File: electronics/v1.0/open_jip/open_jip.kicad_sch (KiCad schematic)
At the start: 28 parts, among them Q1 BSS214NW, U1 OPA355NA, U2 OPA355NA, U3 DAC5571IDBVR, U4 OPA355NA, U5 SeeeduinoXIAO

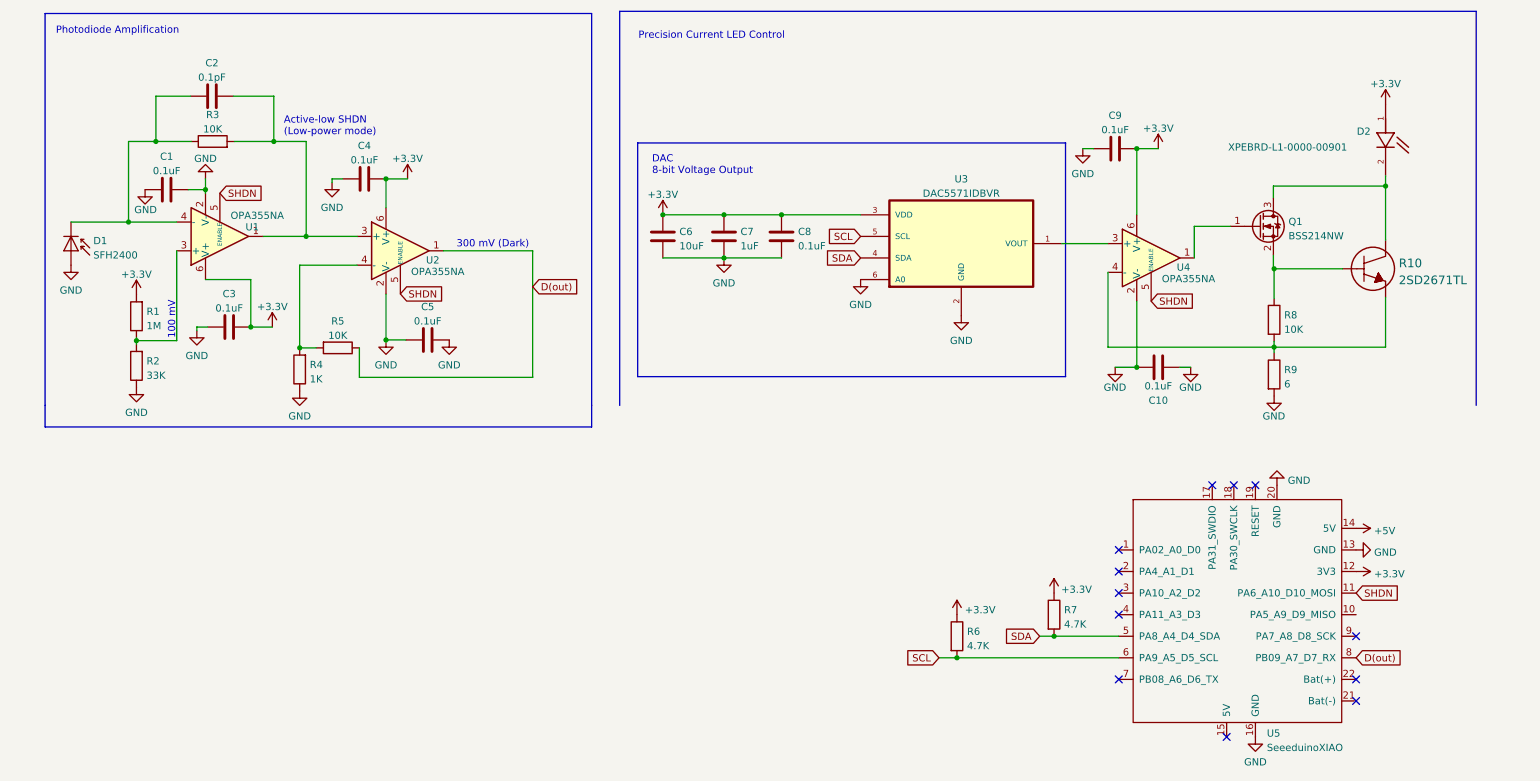
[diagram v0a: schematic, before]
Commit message: added some prelim firmware for v1.0, updated schematic and pcb to remove the second stage trans impedance amplifier on both detection excitation
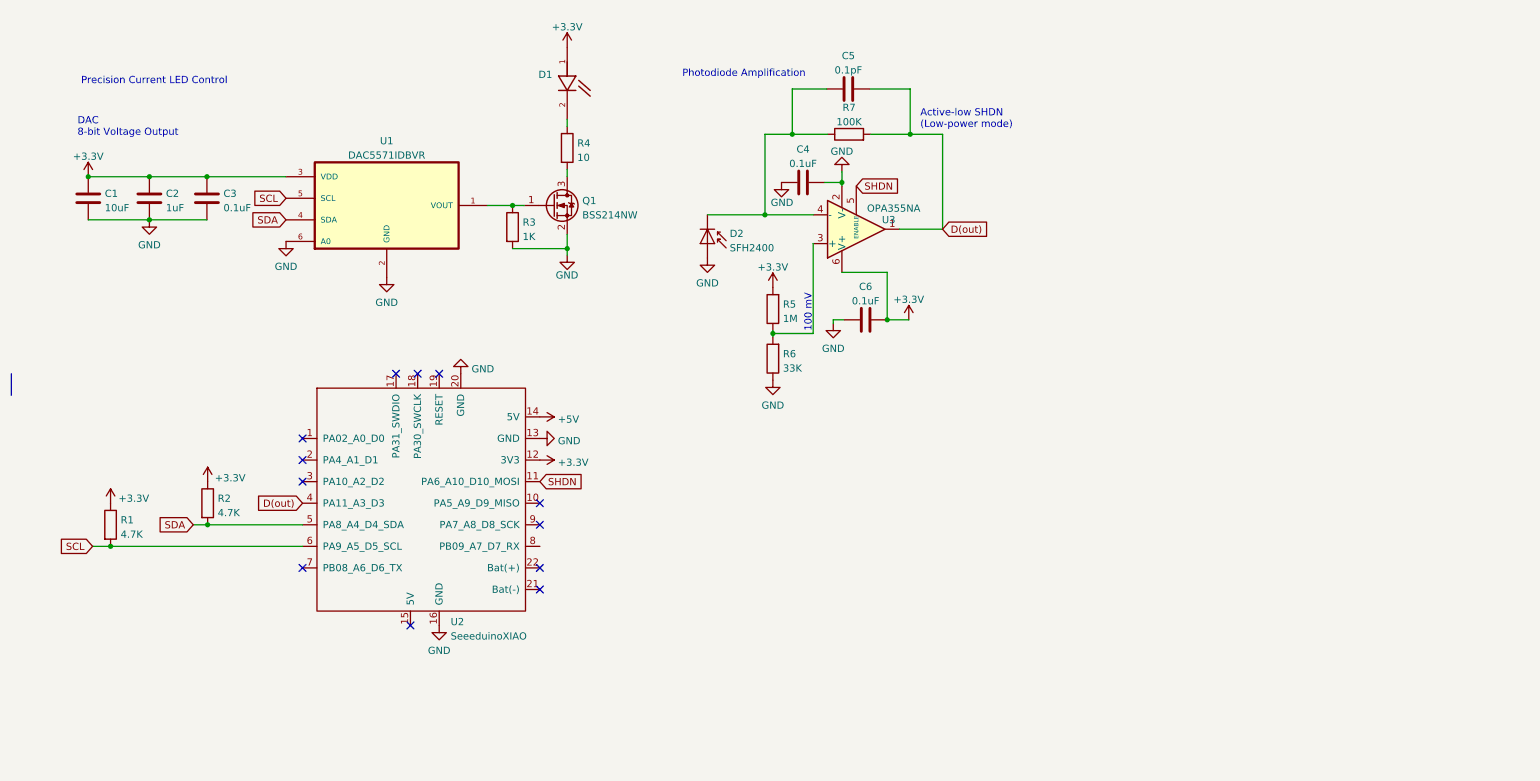
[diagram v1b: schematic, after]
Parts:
- removed C10, C4, C5, C9: 0.1uF, Capacitor_SMD:C_0805_2012Metric, symbol Device:C
- removed R10: 2SD2671TL, 2SD2671TL:2SD2671TL, symbol 2SD2671TL:2SD2671TL
- removed R4: 1K, Resistor_SMD:R_0805_2012Metric, symbol Device:R
- removed R5, R8: 10K, Resistor_SMD:R_0805_2012Metric, symbol Device:R
- removed U2, U4: OPA355NA, Package_TO_SOT_SMD:SOT-23-6, symbol Amplifier_Operational:OPA355NA
- added R3: 1K, Resistor_SMD:R_0805_2012Metric, symbol Device:R
- R4: renamed from R9; value 6 -> 10
- R7: renamed from R3; value 10K -> 100K
- renumbered C6 to C1, C7 to C2, C8 to C3, C1 to C4, C2 to C5, C3 to C6, D2 to D1, D1 to D2, R6 to R1, R7 to R2, R1 to R5, R2 to R6, U3 to U1, U5 to U2, U1 to U3
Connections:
- net D(out): now also C5.2, R7.2, U2.4 (PA11_A3_D3), U3.1; no longer U2.8 (PB09_A7_D7_RX)
- net GND: now also Q1.2 (S), R3.2; no longer R4.2
- net at U1.1 (VOUT): now also Q1.1 (G), R3.1
- net at Q1.3 (D): now also R4.2; no longer D1.2
- net at R4.1: now also D1.2
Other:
- note removed: "300 mV (Dark)"
- moved on the sheet: C1, C2, C3, C4, C5, C6, D1, D2, Q1, R1, R2, R4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

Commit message: sent of two versions to be manufactured, one smd photodiode other with tht
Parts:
- removed C4: 0.1uF, Capacitor_SMD:C_0805_2012Metric, symbol Device:C
- removed D2: SFH2400, OptoDevice:Osram_SMD-SmartDIL, symbol Sensor_Optical:SFH2400
- added D2: SFH_213_FA, SFH_213_FA:XDCR_SFH_213_FA, symbol SFH_213_FA:SFH_213_FA
- R4: value 10 -> 2
- renumbered C5 to C4, C6 to C5
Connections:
- net GND: now also D2.1
- net at C4.1, R7.1, U3.4 (-): now also D2.2
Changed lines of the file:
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@@
   (junction (at 52.197 109.347) (diameter 0) (color 0 0 0 0)
-  )
-  (junction (at 164.211 48.895) (diameter 0) (color 0 0 0 0)
   )
   (junction (at 35.052 113.157) (diameter 0) (color 0 0 0 0)
@@
     (stroke (width 0) (type default) (color 0 0 0 0))
   )
-  (wire (pts (xy 161.163 48.895) (xy 164.211 48.895))
-    (stroke (width 0) (type default) (color 0 0 0 0))
-  )
   (wire (pts (xy 159.131 75.565) (xy 159.131 59.69))
     (stroke (width 0) (type default) (color 0 0 0 0))
@@
     (stroke (width 0) (type default) (color 0 0 0 0))
   )
-  (wire (pts (xy 164.211 48.895) (xy 164.211 49.53))
+  (wire (pts (xy 164.211 46.99) (xy 164.211 49.53))
     (stroke (width 0) (type default) (color 0 0 0 0))
   )
@@
   )
   (wire (pts (xy 176.276 40.386) (xy 181.991 40.386))
-    (stroke (width 0) (type default) (color 0 0 0 0))
-  )
-  (wire (pts (xy 164.211 46.99) (xy 164.211 48.895))
     (stroke (width 0) (type default) (color 0 0 0 0))
   )
@@
   (symbol (lib_id "power:+3.3V") (at 176.022 73.152 0) (unit 1)
     (in_bom yes) (on_board yes) (fields_autoplaced)
-    (property "Reference" "#PWR020" (id 0) (at 176.022 76.962 0)
+    (property "Reference" "#PWR019" (id 0) (at 176.022 76.962 0)
       (effects (font (size 1.27 1.27)) hide)
     )
@@
     (pin "1")
   )
-  (symbol (lib_id "power:GND") (at 140.462 62.23 0) (unit 1)
-    (in_bom yes) (on_board yes) (fields_autoplaced)
-    (property "Reference" "#PWR014" (id 0) (at 140.462 68.58 0)
-      (effects (font (size 1.27 1.27)) hide)
-    )
-    (property "Value" "GND" (id 1) (at 140.462 66.6734 0))
-    (property "Footprint" "" (id 2) (at 140.462 62.23 0)
-      (effects (font (size 1.27 1.27)) hide)
-    )
-    (property "Datasheet" "" (id 3) (at 140.462 62.23 0)
+  (symbol (lib_id "SFH_213_FA:SFH_213_FA") (at 140.462 59.69 90) (unit 1)
+    (in_bom yes) (on_board yes)
+    (property "Reference" "D2" (id 0) (at 142.748 60.7476 90)
+      (effects (font (size 1.27 1.27)) (justify right))
+    )
+    (property "Value" "SFH_213_FA" (id 1) (at 128.397 63.627 90)
+      (effects (font (size 1.27 1.27)) (justify right))
+    )
+    (property "Footprint" "SFH_213_FA:XDCR_SFH_213_FA" (id 2) (at 140.462 59.69 0)
+      (effects (font (size 1.27 1.27)) (justify left bottom) hide)
+    )
+    (property "Datasheet" "" (id 3) (at 140.462 59.69 0)
+      (effects (font (size 1.27 1.27)) (justify left bottom) hide)
+    )
+    (property "PARTREV" "1.3" (id 4) (at 140.462 59.69 0)
+      (effects (font (size 1.27 1.27)) (justify left bottom) hide)
+    )
+    (property "STANDARD" "Manufacturer Recommendations" (id 5) (at 140.462 59.69 0)
+      (effects (font (size 1.27 1.27)) (justify left bottom) hide)
+    )
+    (property "MANUFACTURER" "OSRAM" (id 6) (at 140.462 59.69 0)
+      (effects (font (size 1.27 1.27)) (justify left bottom) hide)
+    )
+    (pin "1")
+    (pin "2")
+  )
+  (symbol (lib_id "power:GND") (at 140.462 67.31 0) (unit 1)
+    (in_bom yes) (on_board yes) (fields_autoplaced)
+    (property "Reference" "#PWR014" (id 0) (at 140.462 73.66 0)
+      (effects (font (size 1.27 1.27)) hide)
+    )
+    (property "Value" "GND" (id 1) (at 140.462 71.7534 0))
+    (property "Footprint" "" (id 2) (at 140.462 67.31 0)
+      (effects (font (size 1.27 1.27)) hide)
+    )
+    (property "Datasheet" "" (id 3) (at 140.462 67.31 0)
       (effects (font (size 1.27 1.27)) hide)
     )
@@
   (symbol (lib_id "Device:C") (at 168.402 73.152 90) (unit 1)
     (in_bom yes) (on_board yes) (fields_autoplaced)
-    (property "Reference" "C6" (id 0) (at 168.402 67.2932 90))
+    (property "Reference" "C5" (id 0) (at 168.402 67.2932 90))
     (property "Value" "0.1uF" (id 1) (at 168.402 69.8301 90))
     (property "Footprint" "Capacitor_SMD:C_0805_2012Metric" (id 2) (at 172.212 72.1868 0)
@@
     (pin "2")
   )
-  (symbol (lib_id "Device:C") (at 157.353 48.895 90) (unit 1)
-    (in_bom yes) (on_board yes) (fields_autoplaced)
-    (property "Reference" "C4" (id 0) (at 157.353 43.0362 90))
-    (property "Value" "0.1uF" (id 1) (at 157.353 45.5731 90))
-    (property "Footprint" "Capacitor_SMD:C_0805_2012Metric" (id 2) (at 161.163 47.9298 0)
-      (effects (font (size 1.27 1.27)) hide)
-    )
-    (property "Datasheet" "~" (id 3) (at 157.353 48.895 0)
-      (effects (font (size 1.27 1.27)) hide)
-    )
-    (pin "1")
-    (pin "2")
-  )
   (symbol (lib_id "power:GND") (at 41.91 55.499 0) (unit 1)
     (in_bom yes) (on_board yes) (fields_autoplaced)
@@
   (symbol (lib_id "power:GND") (at 162.687 73.787 0) (unit 1)
     (in_bom yes) (on_board yes) (fields_autoplaced)
-    (property "Reference" "#PWR018" (id 0) (at 162.687 80.137 0)
+    (property "Reference" "#PWR017" (id 0) (at 162.687 80.137 0)
       (effects (font (size 1.27 1.27)) hide)
     )
@@
       (effects (font (size 1.27 1.27)) (justify left))
     )
-    (property "Value" "10" (id 1) (at 117.475 44.5012 0)
+    (property "Value" "2" (id 1) (at 117.475 44.5012 0)
       (effects (font (size 1.27 1.27)) (justify left))
     )
@@
   (symbol (lib_id "power:GND") (at 164.211 46.99 180) (unit 1)
     (in_bom yes) (on_board yes) (fields_autoplaced)
-    (property "Reference" "#PWR019" (id 0) (at 164.211 40.64 0)
+    (property "Reference" "#PWR018" (id 0) (at 164.211 40.64 0)
       (effects (font (size 1.27 1.27)) hide)
     )
@@
     (pin "1")
   )
-  (symbol (lib_id "power:GND") (at 153.543 48.895 0) (unit 1)
-    (in_bom yes) (on_board yes)
-    (property "Reference" "#PWR017" (id 0) (at 153.543 55.245 0)
-      (effects (font (size 1.27 1.27)) hide)
-    )
-    (property "Value" "GND" (id 1) (at 151.638 52.451 0)
-      (effects (font (size 1.27 1.27)) (justify left))
-    )
-    (property "Footprint" "" (id 2) (at 153.543 48.895 0)
-      (effects (font (size 1.27 1.27)) hide)
-    )
-    (property "Datasheet" "" (id 3) (at 153.543 48.895 0)
-      (effects (font (size 1.27 1.27)) hide)
-    )
-    (pin "1")
-  )
   (symbol (lib_id "Device:R") (at 152.019 71.247 180) (unit 1)
     (in_bom yes) (on_board yes) (fields_autoplaced)
@@
   (symbol (lib_id "Device:C") (at 165.354 32.385 90) (unit 1)
     (in_bom yes) (on_board yes) (fields_autoplaced)
-    (property "Reference" "C5" (id 0) (at 165.354 26.5262 90))
+    (property "Reference" "C4" (id 0) (at 165.354 26.5262 90))
     (property "Value" "0.1pF" (id 1) (at 165.354 29.0631 90))
     (property "Footprint" "Capacitor_SMD:C_0805_2012Metric" (id 2) (at 169.164 31.4198 0)
@@
     (pin "2")
   )
-  (symbol (lib_id "Sensor_Optical:SFH2400") (at 140.462 59.69 270) (unit 1)
-    (in_bom yes) (on_board yes) (fields_autoplaced)
-    (property "Reference" "D2" (id 0) (at 144.399 57.9282 90)
-      (effects (font (size 1.27 1.27)) (justify left))
-    )
-    (property "Value" "SFH2400" (id 1) (at 144.399 60.4651 90)
-      (effects (font (size 1.27 1.27)) (justify left))
-    )
-    (property "Footprint" "OptoDevice:Osram_SMD-SmartDIL" (id 2) (at 144.907 59.69 0)
-      (effects (font (size 1.27 1.27)) hide)
-    )
-    (property "Datasheet" "http://www.osram-os.com/Graphics/XPic5/00215665_0.pdf/SFH%202400.pdf" (id 3) (at 140.462 58.42 0)
-      (effects (font (size 1.27 1.27)) hide)
-    )
-    (pin "1")
-    (pin "2")
-  )
   (symbol (lib_id "power:GND") (at 96.901 82.677 180) (unit 1)
     (in_bom yes) (on_board yes) (fields_autoplaced)
@@
       (reference "#PWR016") (unit 1) (value "GND") (footprint "")
     )
-    (path "/c4f15da1-d0f5-480f-a78b-542842b09f1e"
+    (path "/7f47b8dd-a8c0-41ae-9b72-b78ce88e12a6"
       (reference "#PWR017") (unit 1) (value "GND") (footprint "")
     )
-    (path "/7f47b8dd-a8c0-41ae-9b72-b78ce88e12a6"
+    (path "/c2bbe212-0b25-4de3-a538-71d376b7c02b"
       (reference "#PWR018") (unit 1) (value "GND") (footprint "")
     )
-    (path "/c2bbe212-0b25-4de3-a538-71d376b7c02b"
-      (reference "#PWR019") (unit 1) (value "GND") (footprint "")
-    )
     (path "/07e0c199-f64b-413a-931e-a51b762720eb"
-      (reference "#PWR020") (unit 1) (value "+3.3V") (footprint "")
+      (reference "#PWR019") (unit 1) (value "+3.3V") (footprint "")
     )
     (path "/cb8ec77d-5e14-4fa9-b4f6-f0ee54b27624"
@@
       (reference "C3") (unit 1) (value "0.1uF") (footprint "Capacitor_SMD:C_0805_2012Metric")
     )
-    (path "/7d5a7c11-5209-4ec0-bae8-27899b0984d2"
-      (reference "C4") (unit 1) (value "0.1uF") (footprint "Capacitor_SMD:C_0805_2012Metric")
-    )
     (path "/ebfa6146-9db5-451c-b5a1-b4b7ff347d1f"
-      (reference "C5") (unit 1) (value "0.1pF") (footprint "Capacitor_SMD:C_0805_2012Metric")
+      (reference "C4") (unit 1) (value "0.1pF") (footprint "Capacitor_SMD:C_0805_2012Metric")
     )
     (path "/64d97a90-8ba5-4af6-bfe5-fa4585603603"
-      (reference "C6") (unit 1) (value "0.1uF") (footprint "Capacitor_SMD:C_0805_2012Metric")
+      (reference "C5") (unit 1) (value "0.1uF") (footprint "Capacitor_SMD:C_0805_2012Metric")
     )
     (path "/afdb278b-fd32-4940-bf81-4b7b3a607866"
       (reference "D1") (unit 1) (value "XPEBRD-L1-0000-00901") (footprint "XPEBRD-L1-0000-00901:LED_XPEBRD-L1-0000-00901")
     )
-    (path "/f6698be2-2e7a-48d4-9274-3e570a137747"
-      (reference "D2") (unit 1) (value "SFH2400") (footprint "OptoDevice:Osram_SMD-SmartDIL")
+    (path "/376e1af9-0fa2-4967-911e-efe2c5d61d46"
+      (reference "D2") (unit 1) (value "SFH_213_FA") (footprint "SFH_213_FA:XDCR_SFH_213_FA")
     )
     (path "/5f837a81-729c-4e1c-aa97-975c6f16bd4b"
@@
     )
     (path "/a733e5e9-7218-469a-8bb3-b959920baaa0"
-      (reference "R4") (unit 1) (value "10") (footprint "Resistor_SMD:R_2512_6332Metric")
+      (reference "R4") (unit 1) (value "2") (footprint "Resistor_SMD:R_2512_6332Metric")
     )
     (path "/c8cd6e27-b3f2-466d-8c57-30a82e5ce276"

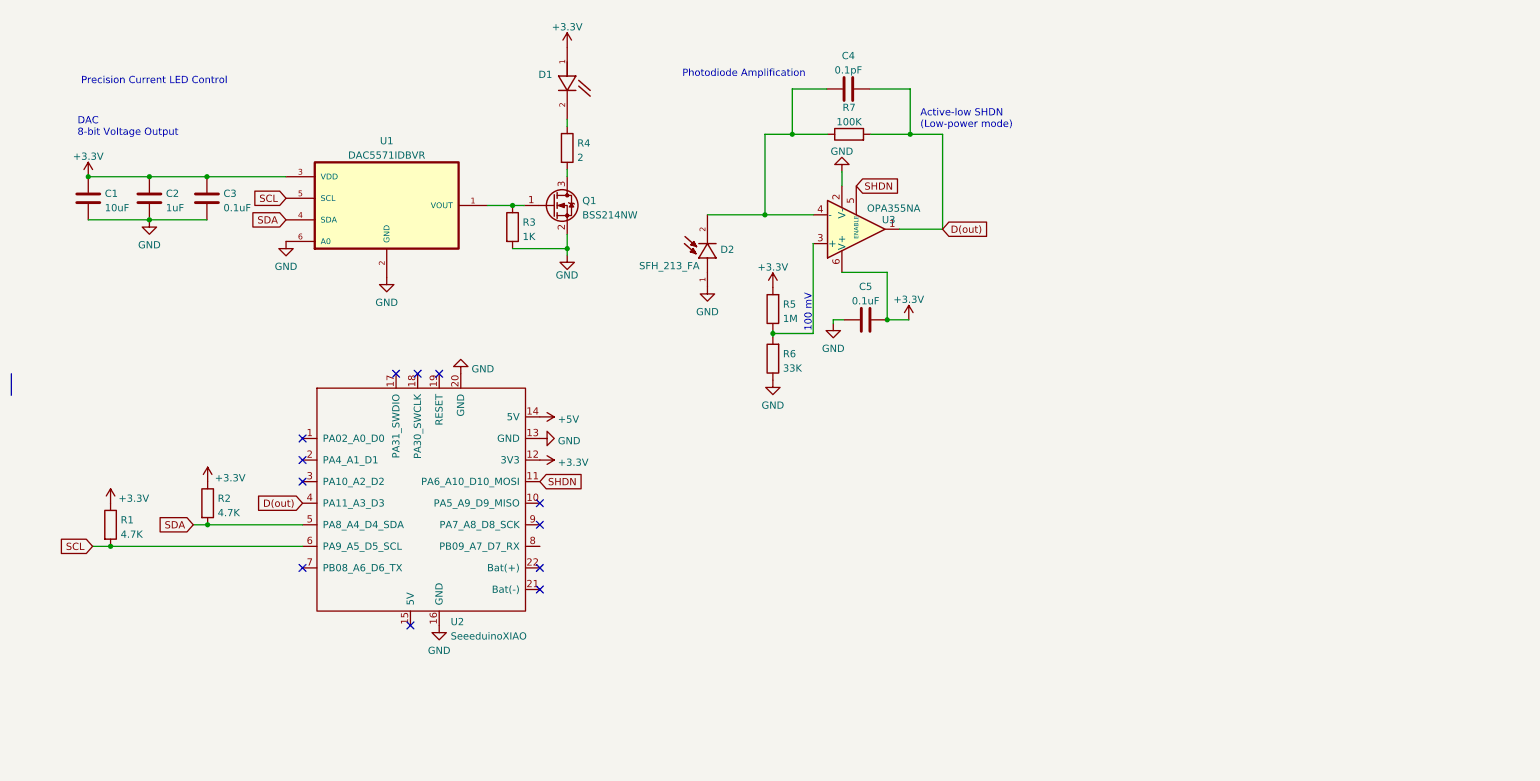
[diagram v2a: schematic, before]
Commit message: updates to version 1.0 with 18650 and new power supply
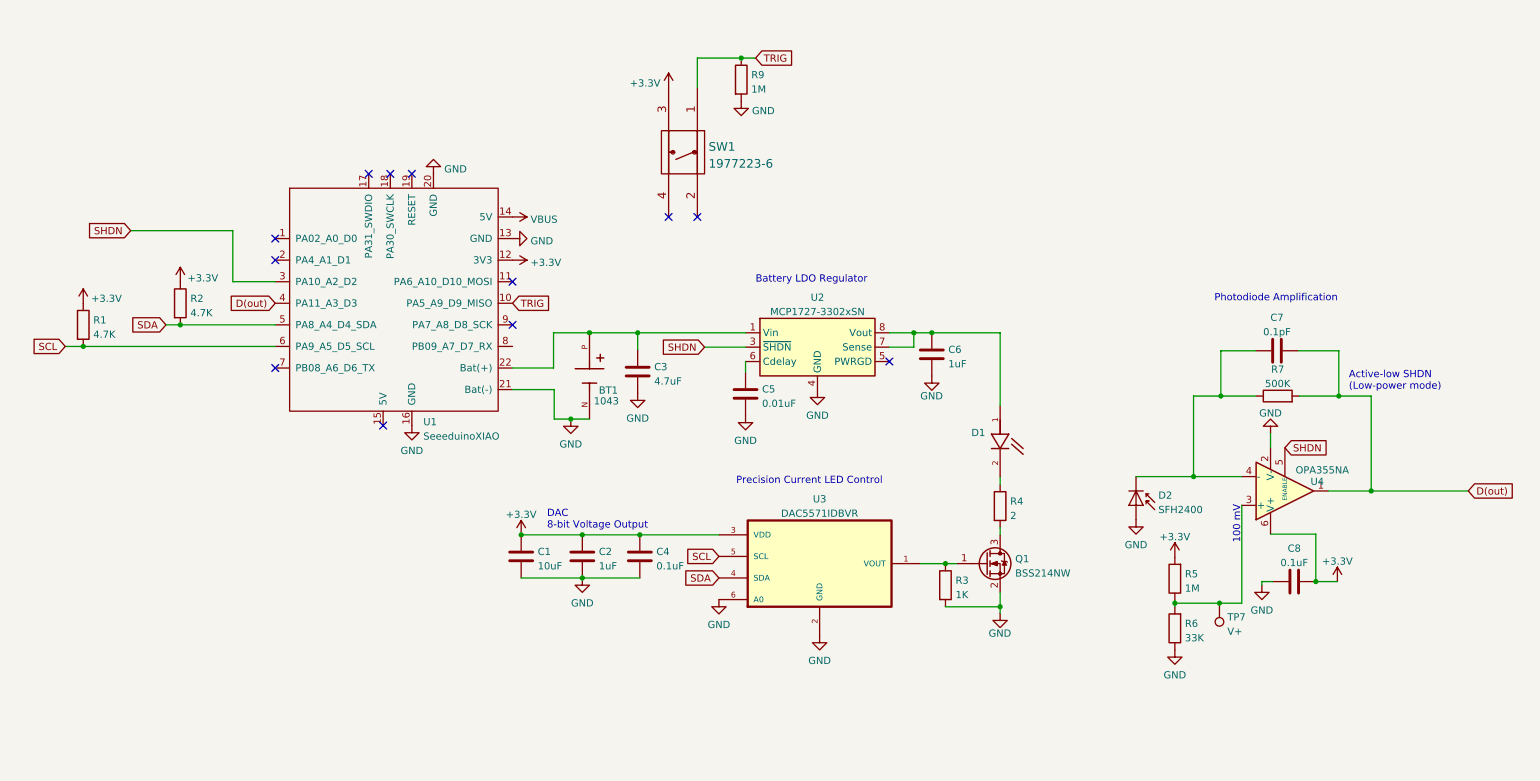
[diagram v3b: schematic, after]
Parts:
- removed D2: SFH_213_FA, SFH_213_FA:XDCR_SFH_213_FA, symbol SFH_213_FA:SFH_213_FA
- added BT1: 1043, 1043:BAT_1043, symbol 1043:1043
- added C3: 4.7uF, Capacitor_SMD:C_0805_2012Metric, symbol Device:C
- added C5: 0.01uF, Capacitor_SMD:C_0805_2012Metric, symbol Device:C
- added C6: 1uF, Capacitor_SMD:C_0805_2012Metric, symbol Device:C
- added D2: SFH2400, OptoDevice:Osram_SMD-SmartDIL, symbol Sensor_Optical:SFH2400
- added R9: 1M, Resistor_SMD:R_0805_2012Metric, symbol Device:R
- added SW1: 1977223-6, 1977223-6:1977223-6, symbol 2022-10-04_00-56-22:1977223-6
- added TP7: V+, TestPoint:TestPoint_Pad_D1.5mm, symbol Connector:TestPoint
- added U2: MCP1727-3302xSN, Package_SO:SOIC-8_3.9x4.9mm_P1.27mm, symbol Regulator_Linear:MCP1727-3302xSN
- R7: value 100K -> 500K
- renumbered C3 to C4, C4 to C7, C5 to C8, U2 to U1, U1 to U3, U3 to U4
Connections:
- net +3.3V: now also SW1.3; no longer D1.1
- net GND: now also U1.21 (Bat(-)), BT1.N, C3.2, C5.2, C6.2, D2.3 (A), R9.2, U2.4 (GND)
- net SHDN: now also U1.3 (PA10_A2_D2), U2.3 (~{SHDN}); no longer U1.11 (PA6_A10_D10_MOSI)
- net at C7.1, R7.1, U4.4 (-): now also D2.1 (C)
- net at R5.1, R6.2, U4.3 (+): now also TP7.1
- net TRIG: now reaches U1.10 (PA5_A9_D9_MISO)
- net TRIG: now also R9.1, SW1.1
- net at U1.22 (Bat(+)): now also BT1.P, C3.1, U2.1 (Vin), U2.2 (Vin)
- net +5V renamed VBUS
- new net: C6.1, D1.1, U2.7 (Sense), U2.8 (Vout)
- new net: C5.1, U2.6 (Cdelay)
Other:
- note added: "Battery LDO Regulator"
- moved on the sheet: C1, C2, C4, C7, C8, D1, Q1, R1, R2, R3, R4, R5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
